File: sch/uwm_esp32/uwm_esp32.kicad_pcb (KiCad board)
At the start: 2 copper layers, 85.6 x 54 mm, 25 parts, among them J1 ESP32 Edge Header, J2 DWM Edge Header, SW1 Sleep Button, U1 XIAO_ESP32C3, U2 DWM3000TR13

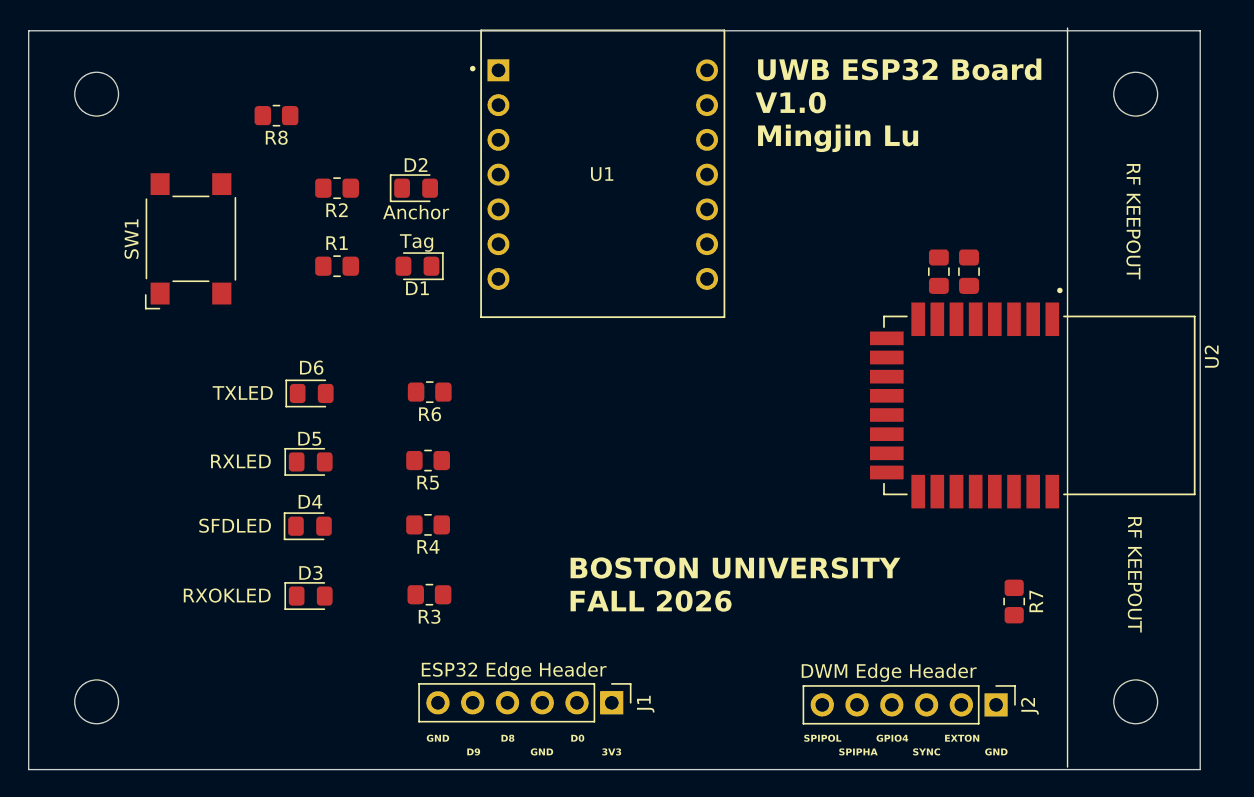
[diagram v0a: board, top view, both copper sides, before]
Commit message: Route ESP32 board and add ground pour
Add signal and power routing with vias and filled ground zones. Rotate and unlock R1 to match the updated layout.
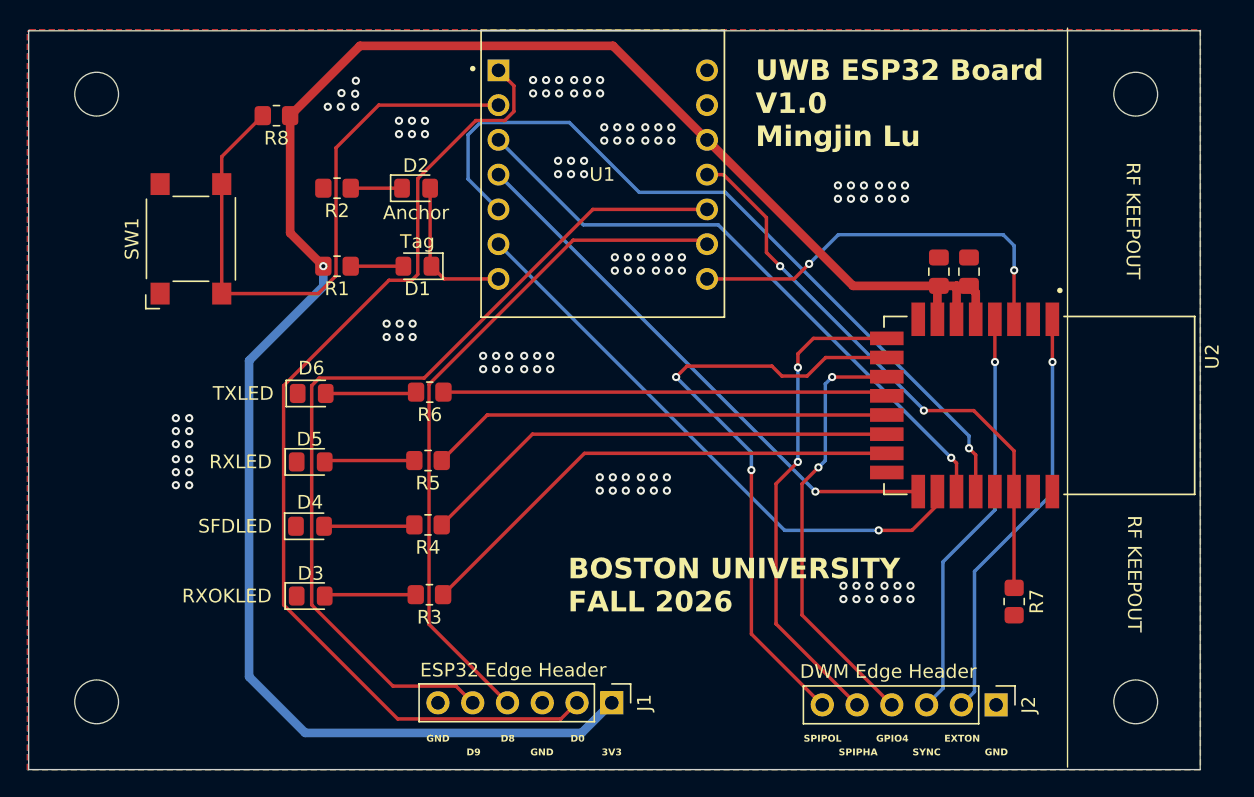
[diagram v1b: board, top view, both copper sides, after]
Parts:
- turned R1 to 180 degrees
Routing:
- net +3V3: track 0.00 -> 139.9 mm, vias 0 -> 1
- net /D0: track 0.00 -> 74.1 mm
- net /D9: track 0.00 -> 65.0 mm
- net /SPICLK: track 0.00 -> 57.1 mm, vias 0 -> 1
- net /D8: track 0.00 -> 50.6 mm
- net Net-(U1-D1): track 0.00 -> 46.0 mm
- net /SPIMISO: track 0.00 -> 45.3 mm, vias 0 -> 1
- net /SPIPOL: track 0.00 -> 45.1 mm, vias 0 -> 2
- net /IRQ: track 0.00 -> 42.6 mm, vias 0 -> 2
- net /SPIMOSI: track 0.00 -> 42.5 mm, vias 0 -> 1
- net /SPICSn: track 0.00 -> 40.3 mm, vias 0 -> 1
- net /RXOKLED: track 0.00 -> 36.7 mm
- net /SPIPHA: track 0.00 -> 35.7 mm, vias 0 -> 2
- net /SFDLED: track 0.00 -> 35.3 mm
- net /RXLED: track 0.00 -> 33.9 mm
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- added copper zone on B.Cu, net GND
- added copper zone on F.Cu, net GND
